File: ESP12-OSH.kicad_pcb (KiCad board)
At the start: 2 copper layers, 58.8 x 52.1 mm, 14 parts, among them P1 CONN_01X08, P2 CONN_01X06, P3 CONN_01X08, P4 CONN_01X02, U2 ESP-12E, U3 SPX2920U-3.3

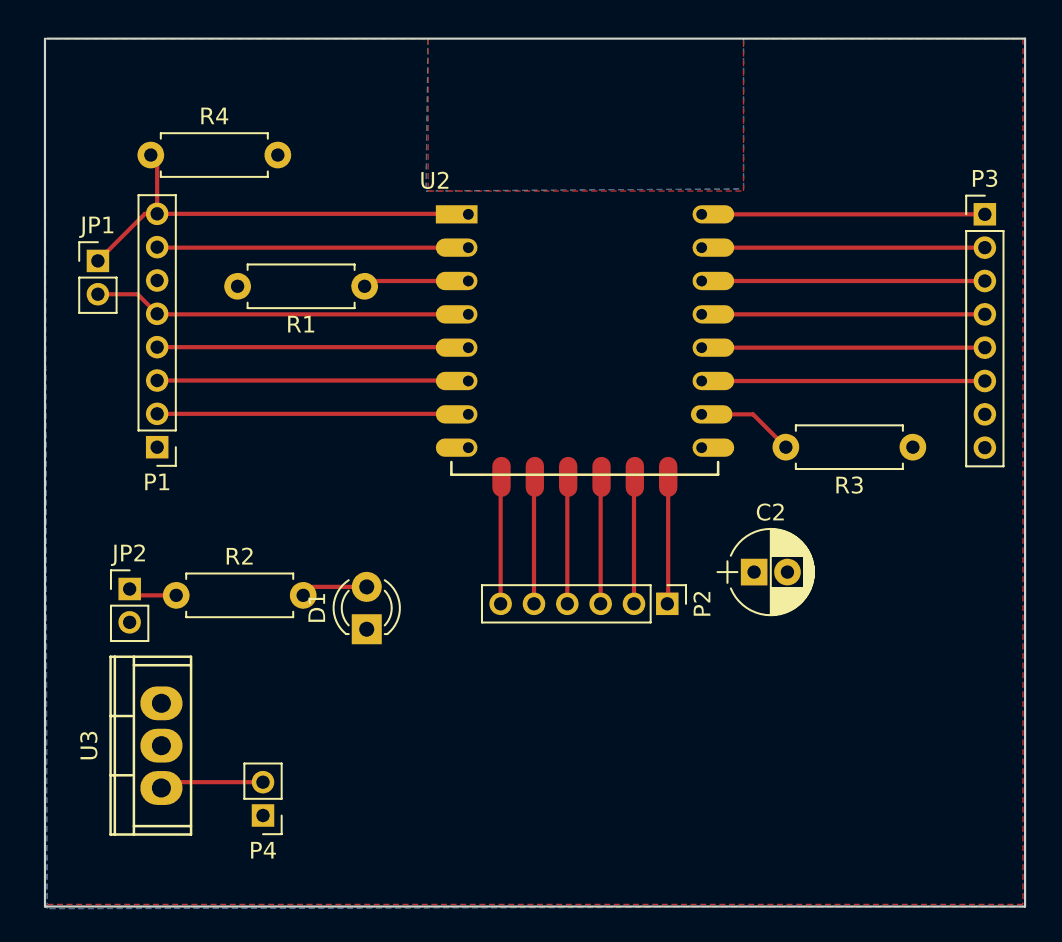
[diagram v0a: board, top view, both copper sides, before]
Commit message: headers with 2.54mm spacing
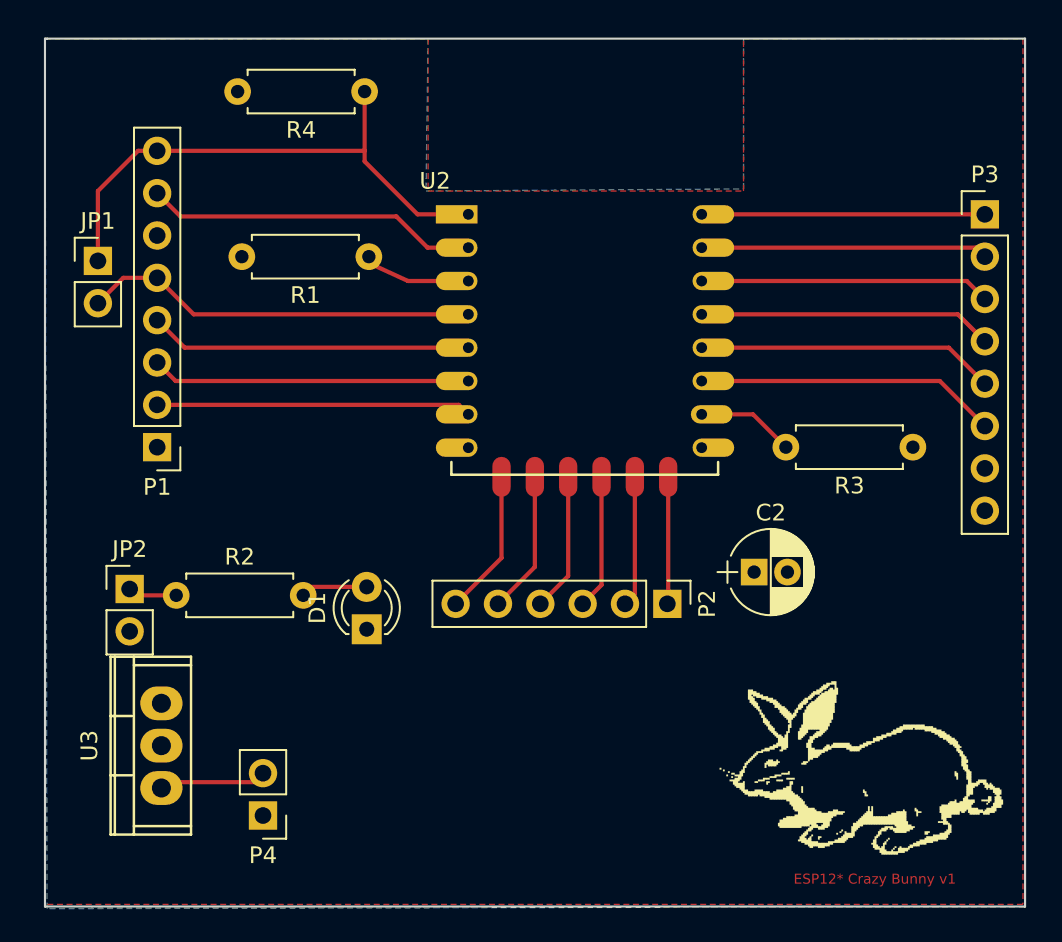
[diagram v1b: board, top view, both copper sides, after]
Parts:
- added LOGO: , ESP12:newlogo, F.Cu at (156.3, 105.5)
- JP1, JP2, P4: footprint Pin_Headers:Pin_Header_Straight_1x02_Pitch2.00mm -> Pin_Headers:Pin_Header_Straight_1x02_Pitch2.54mm
- P1, P3: footprint Pin_Headers:Pin_Header_Straight_1x08_Pitch2.00mm -> Pin_Headers:Pin_Header_Straight_1x08_Pitch2.54mm
- P2: footprint Pin_Headers:Pin_Header_Straight_1x06_Pitch2.00mm -> Pin_Headers:Pin_Header_Straight_1x06_Pitch2.54mm
- moved R4 13.4 mm to (135.6, 70.4), turned to 180 degrees
- moved R1 1.80 mm to (135.9, 80.3)
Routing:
- net Net-(JP1-Pad1): track 27.1 -> 32.9 mm
- net Net-(P1-Pad7): track 18.7 -> 20.0 mm
- net Net-(P2-Pad6): track 7.64 -> 8.83 mm
- net Net-(P3-Pad6): track 17.0 -> 18.1 mm
- net Net-(JP1-Pad2): track 22.7 -> 23.8 mm
- net Net-(P2-Pad5): track 7.64 -> 8.61 mm
- net Net-(P3-Pad5): track 17.0 -> 17.9 mm
- net Net-(P1-Pad4): track 18.7 -> 19.4 mm
- net Net-(P2-Pad4): track 7.64 -> 8.38 mm
- net Net-(P3-Pad4): track 17.0 -> 17.7 mm
- net Net-(P2-Pad3): track 7.64 -> 8.16 mm
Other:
- board text added: "ESP12* Crazy Bunny v1"

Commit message: commit before SO question
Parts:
- removed LOGO: , ESP12:newlogo
- moved P4 59.7 mm to (172.3, 72.1)
- moved U3 56.4 mm to (164.6, 71.0), turned to 0 degrees
- moved JP1 16.3 mm to (132.0, 69.8)
- moved D1 14.0 mm to (123.4, 95.9)
- moved R1 11.8 mm to (126.2, 73.4)
- moved JP2 11.6 mm to (133.1, 101.1), turned to 90 degrees
- moved R4 9.42 mm to (126.2, 69.7)
- moved R2 7.86 mm to (128.4, 93.9)
- moved P1 5.76 mm to (118.9, 95.5)
- moved P3 0.13 mm to (172.7, 77.7)
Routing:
- net Net-(JP1-Pad2): track 23.8 -> 43.1 mm, vias 0 -> 2
- net Net-(R1-Pad1): track 6.59 -> 24.1 mm, vias 0 -> 1
- net Net-(D1-Pad2): track 4.02 -> 16.5 mm
- net Net-(P4-Pad2): track 6.24 -> 15.5 mm
- net Net-(JP1-Pad1): track 32.9 -> 41.7 mm
- net Net-(JP2-Pad1): track 2.95 -> 9.43 mm
- net Net-(P1-Pad2): track 18.9 -> 24.3 mm
- net Net-(P1-Pad3): track 19.2 -> 24.2 mm
- net Net-(P1-Pad4): track 19.4 -> 23.9 mm
- net Net-(P1-Pad7): track 20.0 -> 23.2 mm
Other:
- board size 58.8 x 52.1 mm -> 59.6 x 40.5 mm
- board text added: "ESP12 Breakout v1"
- board text removed: "ESP12* Crazy Bunny v1"

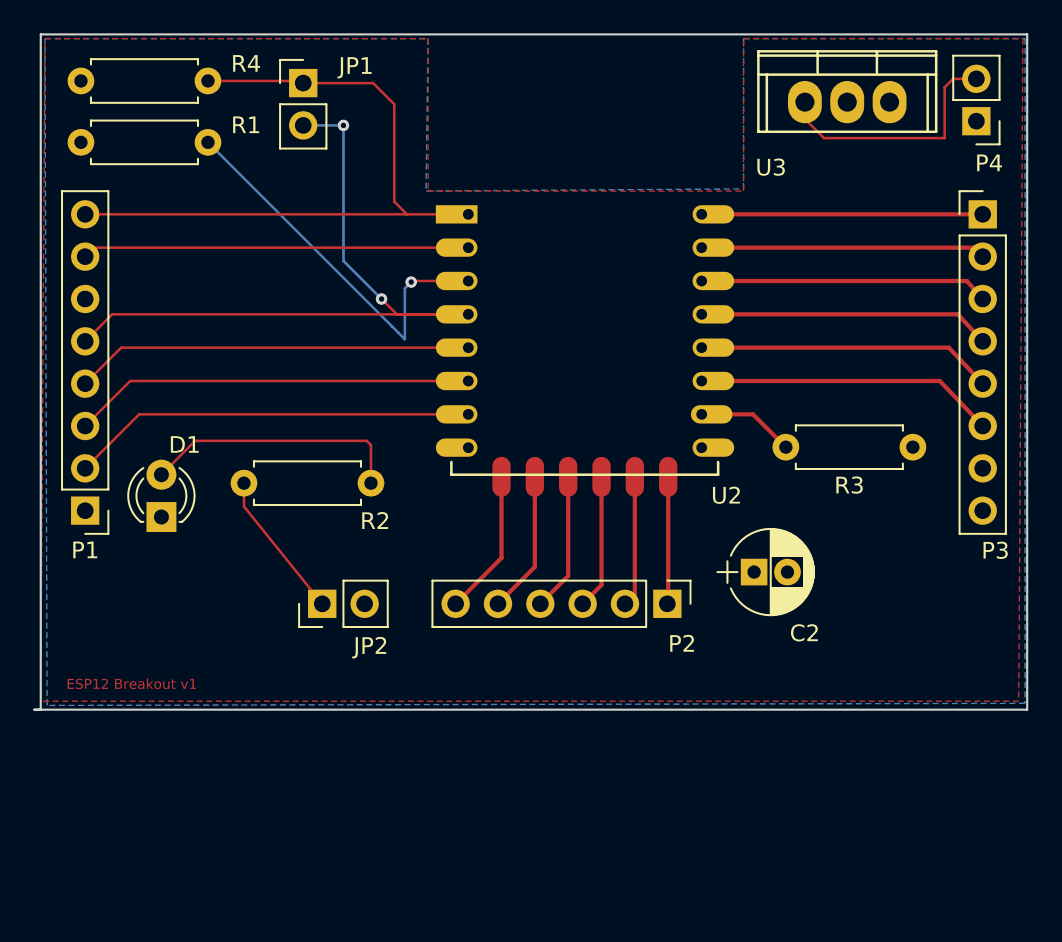
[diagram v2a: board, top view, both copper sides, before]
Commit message: extra small cap, moved large cap, removed front zone VCC, removed vias, moved parts around, added mounting holes
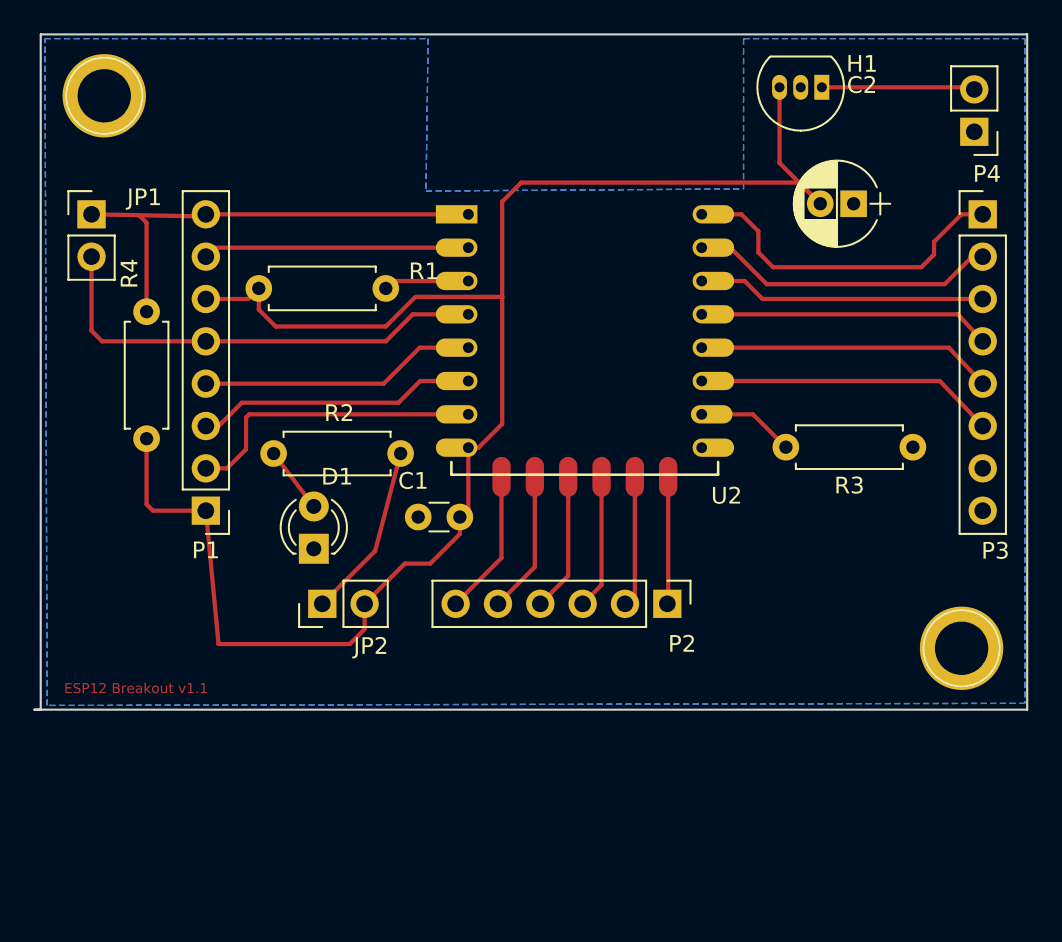
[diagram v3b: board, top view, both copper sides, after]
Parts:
- removed U3: SPX2920U-3.3, Power_Integrations:TO-220
- added C1: 100nF, Capacitors_THT:C_Disc_D3.0mm_W1.6mm_P2.50mm, F.Cu at (141.4, 95.9)
- added H1: HT7333, TO_SOT_Packages_THT:TO-92_Inline_Narrow_Oval, F.Cu at (163.1, 70.1)
- added REF**: 1pin, Connectors:1pin, F.Cu at (171.4, 103.8)
- added REF**: 1pin, Connectors:1pin, F.Cu at (120.0, 70.6)
- moved C2 22.9 mm to (165.0, 77.1), turned to 180 degrees
- moved JP1 14.9 mm to (119.3, 77.7)
- moved R4 14.3 mm to (122.6, 83.6), turned to 270 degrees
- moved R1 13.8 mm to (136.9, 82.2)
- moved R2 9.56 mm to (137.8, 92.1), turned to 180 degrees
- moved D1 9.34 mm to (132.6, 97.8)
- moved P1 7.24 mm to (126.1, 95.5)
- moved P4 0.65 mm to (172.2, 72.8)
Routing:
- net /VCC: track 0.04 -> 103.7 mm
- net Net-(R1-Pad1): track 24.1 -> 5.14 mm, vias 1 -> 0
- net Net-(JP1-Pad2): track 43.1 -> 28.0 mm, vias 2 -> 0
- net Net-(JP1-Pad1): track 41.7 -> 28.6 mm
- net Net-(D1-Pad2): track 16.5 -> 3.99 mm
- net Net-(P1-Pad4): track 23.9 -> 16.7 mm
- net Net-(P1-Pad3): track 24.2 -> 17.0 mm
- net Net-(P1-Pad7): track 23.2 -> 16.7 mm
- net Net-(P1-Pad2): track 24.3 -> 18.2 mm
- net Net-(H1-Pad1): track 15.5 -> 9.69 mm
- net /TX: track 16.9 -> 20.7 mm
- net Net-(JP2-Pad1): track 9.43 -> 11.8 mm
- net /RX: track 17.1 -> 19.2 mm
- removed copper zone on F.Cu, net /VCC
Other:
- board text added: "ESP12 Breakout v1.1"
- board text removed: "ESP12 Breakout v1"
